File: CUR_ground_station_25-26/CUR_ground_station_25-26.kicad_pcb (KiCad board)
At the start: 4 copper layers, 74 x 58.6 mm, 84 parts, among them J1 Conn_01x02, J2 UJ20-C-H-G-SMT-P16-TR, J3 Conn_Coaxial_Small, J4 Conn_01x04_Pin, Q1 NTR4003N, Q2 NTR4003N, SW1 PTS815SJM250SMTRLFS, SW2 PTS815SJM250SMTRLFS, SW3 PTS815SJM250SMTRLFS, SW4 PTS815SJM250SMTRLFS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

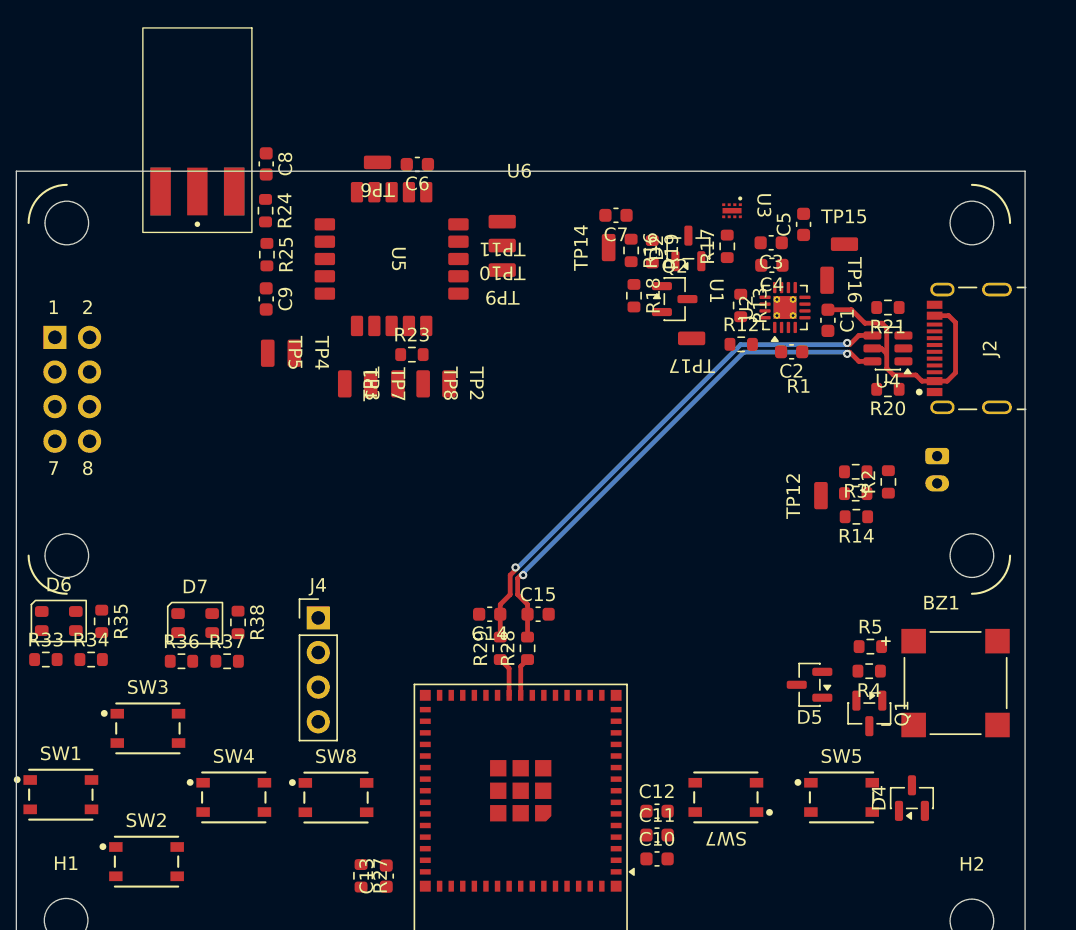
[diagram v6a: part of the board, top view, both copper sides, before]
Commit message: routing power section
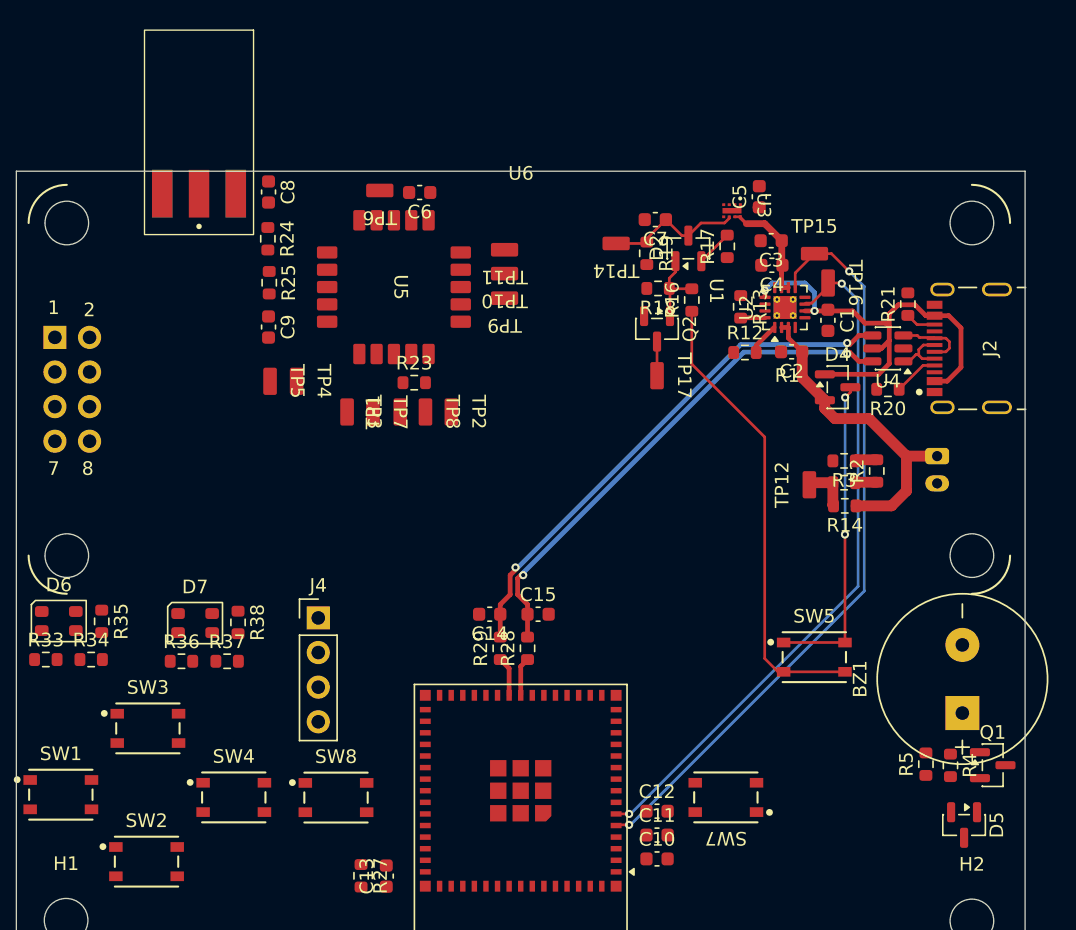
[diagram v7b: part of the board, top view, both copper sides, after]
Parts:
- BZ1: footprint Buzzer_SameSky:XDCR_CMT-7525-03-SMT-TR -> Buzzer_SameSky:Buzzer_SameSky_CPT-1207-3TH
- moved D4 30.6 mm to (108.8, 65.8), turned to 0 degrees
- moved D5 15.3 mm to (118.0, 98.0), turned to -90 degrees
- moved SW5 10.5 mm to (107.0, 85.7)
- moved Q1 9.82 mm to (120.1, 93.6), turned to 0 degrees
- moved R5 9.54 mm to (115.2, 93.5), turned to 90 degrees
- moved R4 9.13 mm to (117.0, 93.6), turned to -90 degrees
- moved R16 5.75 mm to (98.0, 59.5), turned to 90 degrees
- moved C5 3.83 mm to (103.0, 51.9)
- moved TP17 3.73 mm to (95.5, 65.0), turned to -90 degrees
- moved C7 2.90 mm to (95.4, 53.5)
- moved Q2 2.54 mm to (95.5, 61.6), turned to -90 degrees
- moved TP15 2.31 mm to (107.0, 56.0)
- moved C6 2.07 mm to (78.1, 51.6)
- moved C9 2.07 mm to (67.0, 61.4)
- moved R23 2.07 mm to (77.7, 65.5)
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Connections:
- U1 pad 7: /MCU/PWR_BTN -> /MCU/PWR_EN
- U1 pad 8: /MCU/PWR_EN -> /MCU/PWR_BTN
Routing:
- net /MCU/~{CHG}: track 0.00 -> 55.4 mm, vias 0 -> 2
- net /MCU/~{PGOOD}: track 0.00 -> 50.9 mm, vias 0 -> 2
- net Net-(R16-Pad1): track 0.00 -> 34.1 mm
- net +BATT: track 0.17 -> 24.1 mm
- net Net-(D4-Pad3): track 0.00 -> 23.4 mm, vias 0 -> 2
- net VBUS: track 20.2 -> 34.2 mm, vias 0 -> 2
- net /Power/LDO_EN: track 0.00 -> 10.3 mm
- net IN: track 0.17 -> 8.38 mm
- net Net-(Q2-G): track 0.00 -> 5.48 mm
- net Net-(J2-D+-PadA6): track 0.00 -> 5.24 mm
- net Net-(J2-D--PadA7): track 0.00 -> 4.31 mm
- net /MCU/BATT_VSENSE: track 0.00 -> 3.51 mm
- net Net-(J2-CC1): track 0.00 -> 3.32 mm
- net Net-(D2-Pad2): track 0.00 -> 2.70 mm
- net /MCU/PWR_BTN: track 0.00 -> 2.50 mm
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
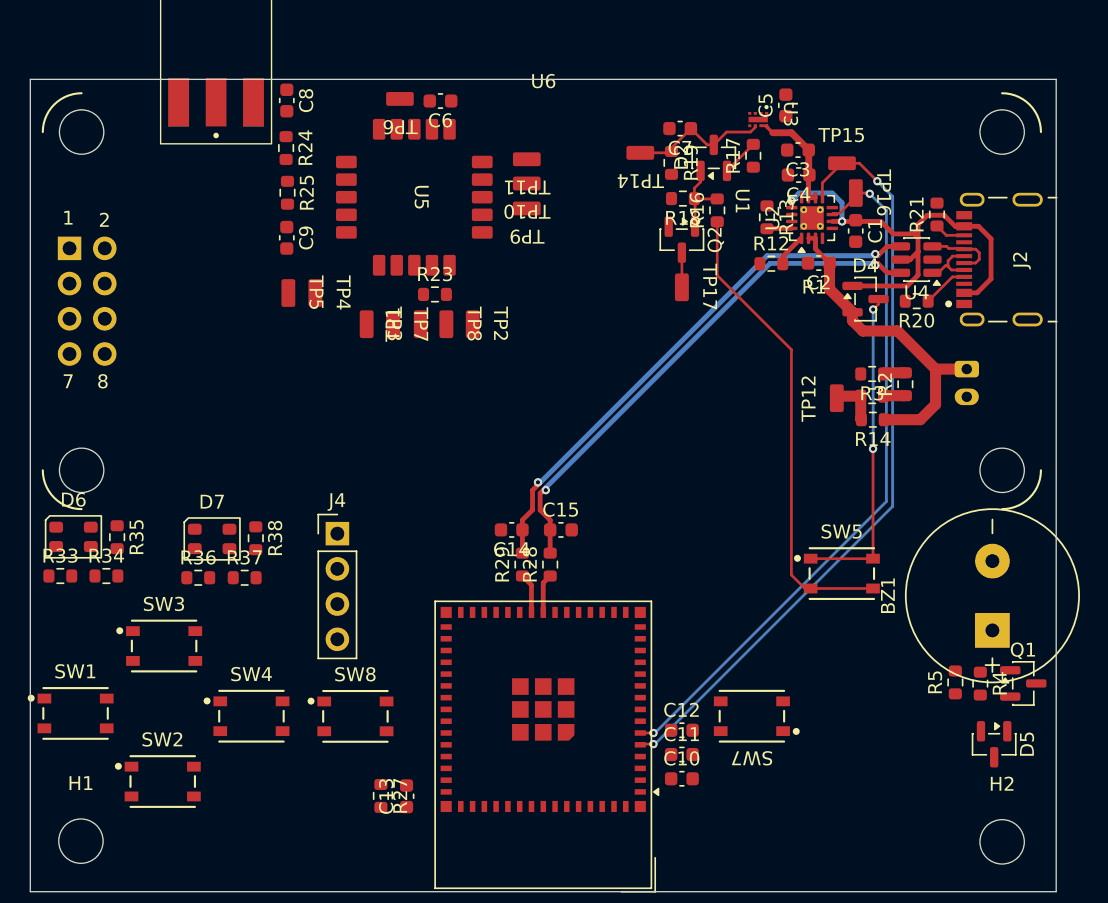
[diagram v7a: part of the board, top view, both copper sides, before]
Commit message: preliminary 3v3 rail routed
routed on top layer. Its...interesting...
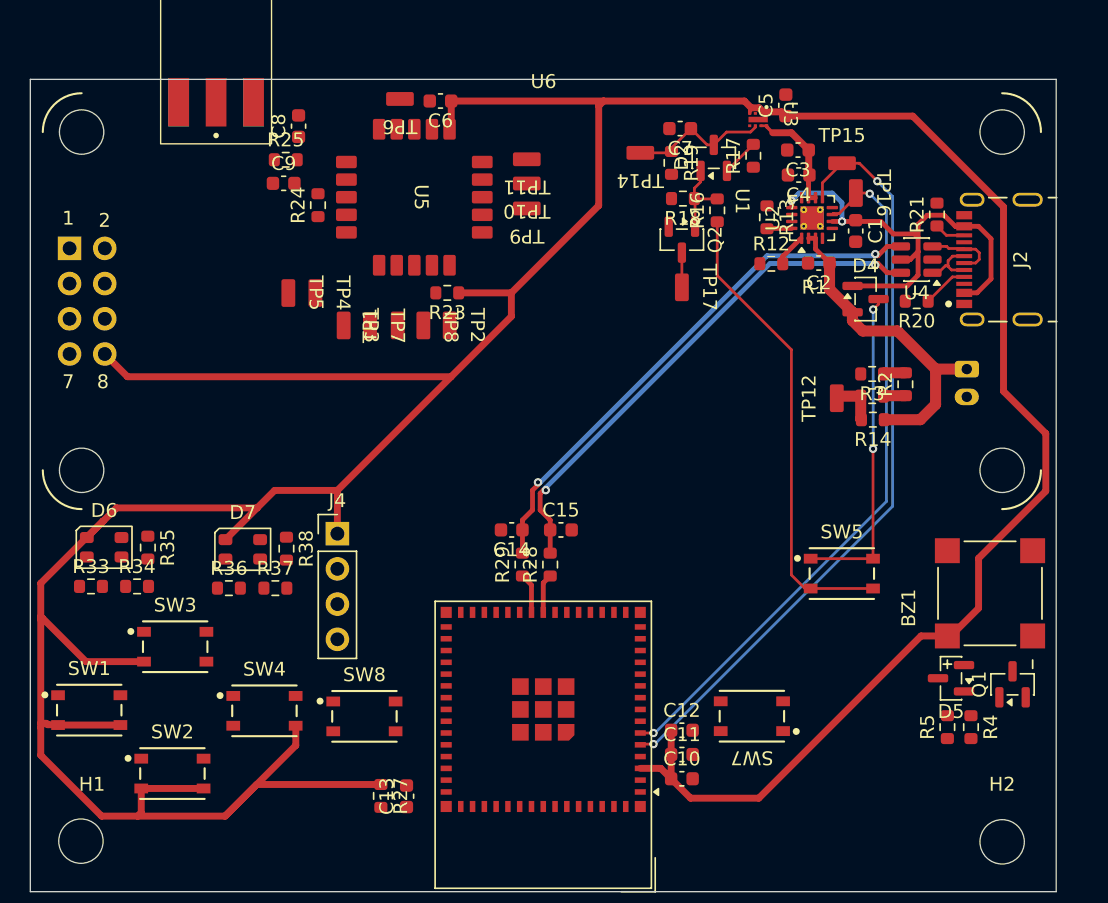
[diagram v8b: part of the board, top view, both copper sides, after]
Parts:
- BZ1: footprint Buzzer_SameSky:Buzzer_SameSky_CPT-1207-3TH -> Buzzer_SameSky:XDCR_CMT-7525-03-SMT-TR
- moved D5 5.69 mm to (114.9, 93.2), turned to 180 degrees
- moved R24 4.72 mm to (69.2, 59.1), turned to 90 degrees
- moved C9 3.94 mm to (66.8, 57.5), turned to 0 degrees
- moved R5 3.28 mm to (114.7, 96.7)
- moved R4 3.21 mm to (116.3, 96.7)
- moved R25 2.38 mm to (66.9, 55.8), turned to 0 degrees
- moved D6 2.34 mm to (53.8, 83.7)
- moved D7 2.34 mm to (63.8, 83.9)
- moved R34 2.34 mm to (56.2, 86.6)
- moved R36 2.34 mm to (62.8, 86.7)
- moved R33 2.34 mm to (52.9, 86.6)
- moved R35 2.34 mm to (57.0, 83.8)
- moved R37 2.34 mm to (66.2, 86.7)
- moved R38 2.34 mm to (67.0, 83.8)
- moved C8 2.04 mm to (67.8, 53.4), turned to 90 degrees
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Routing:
- net +3V3: track 0.25 -> 279.6 mm
